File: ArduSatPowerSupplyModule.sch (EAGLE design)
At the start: 167 parts, among them IC1 AVR-MEGA8-MI, IC10 TMP102, IC11 TMP102, IC2 ATMEGA16U2-MU, IC3 LTC3115, IC4 LTC4078, IC5 MAX17043G+U, IC6 MAX4372F, IC7 LTC3536, IC8 MAX4372F, IC9 LTC3536, Q1 RJU003N03 N-MOSFET, Q2 RJU003N03 N-MOSFET, Q3 MOSFET-PCHANNELSMT2, Q4 RJU003N03 N-MOSFET, Q5 RJU003N03 N-MOSFET, Q6 RJU003N03 N-MOSFET, Q7 RJU003N03 N-MOSFET, Q8 RJU003N03 N-MOSFET, Q9 RJU003N03 N-MOSFET, SW1 RESET, SW2 SWITCH-SPDT

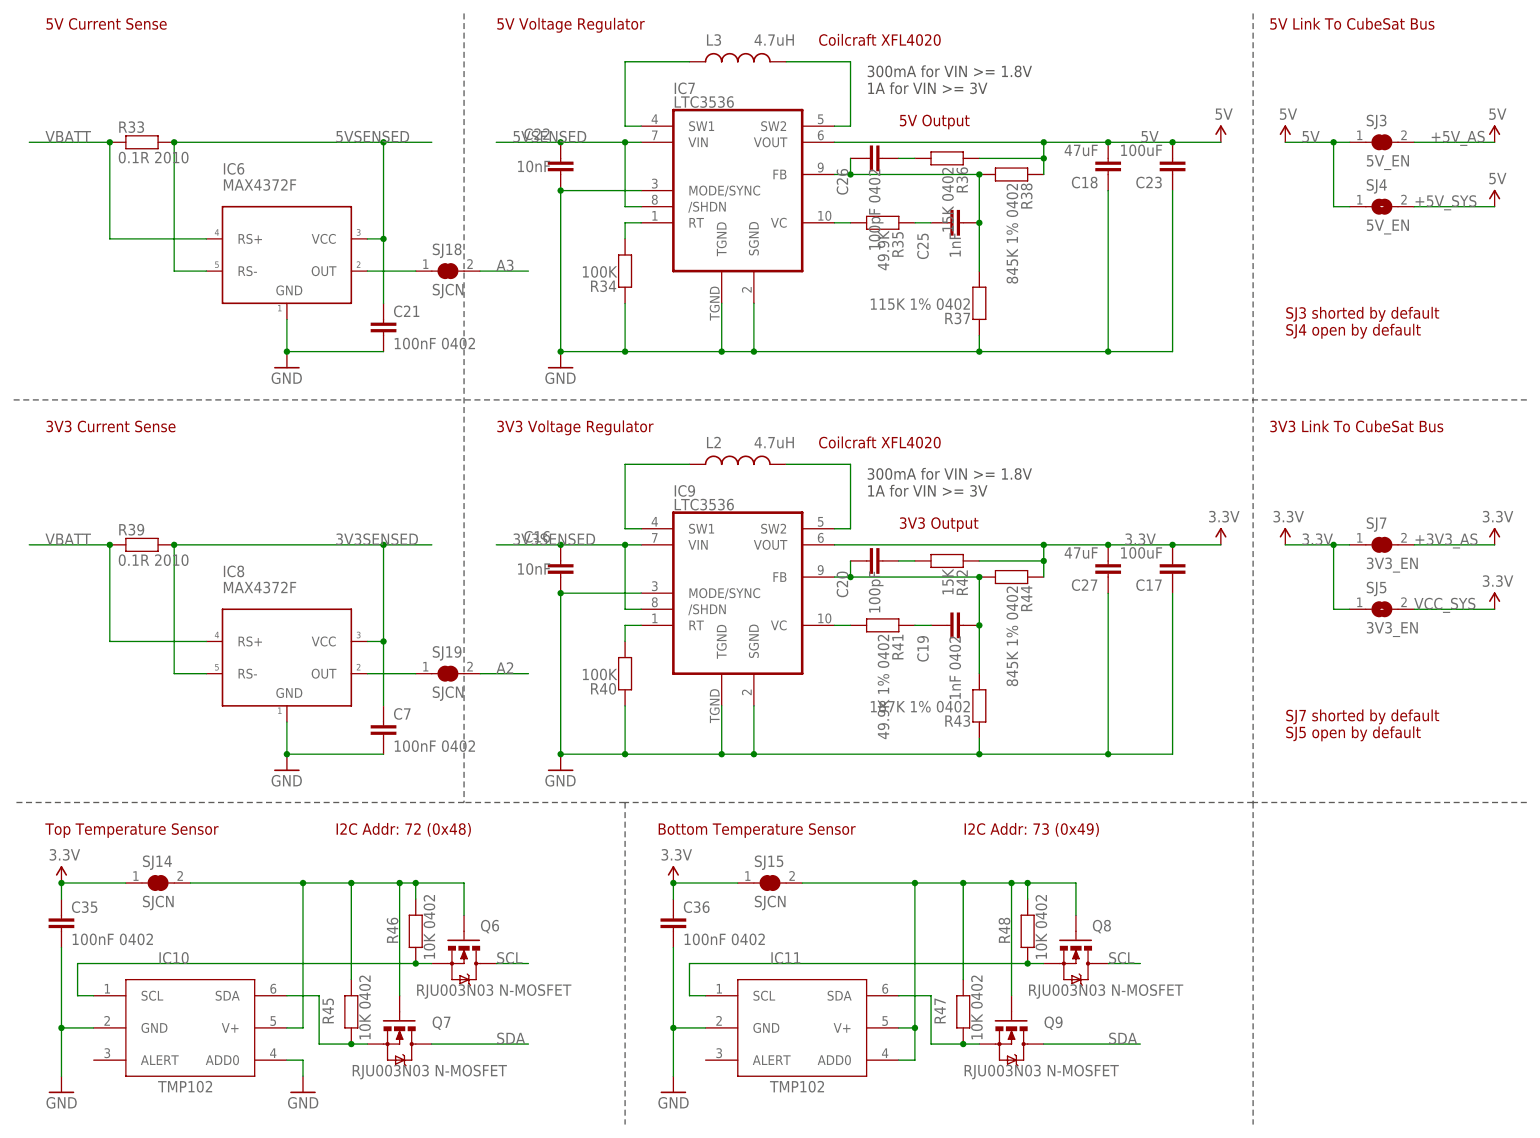
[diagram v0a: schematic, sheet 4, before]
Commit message: Changed max charge rate to 1A; removed solder jumpers for ArduSat power pins
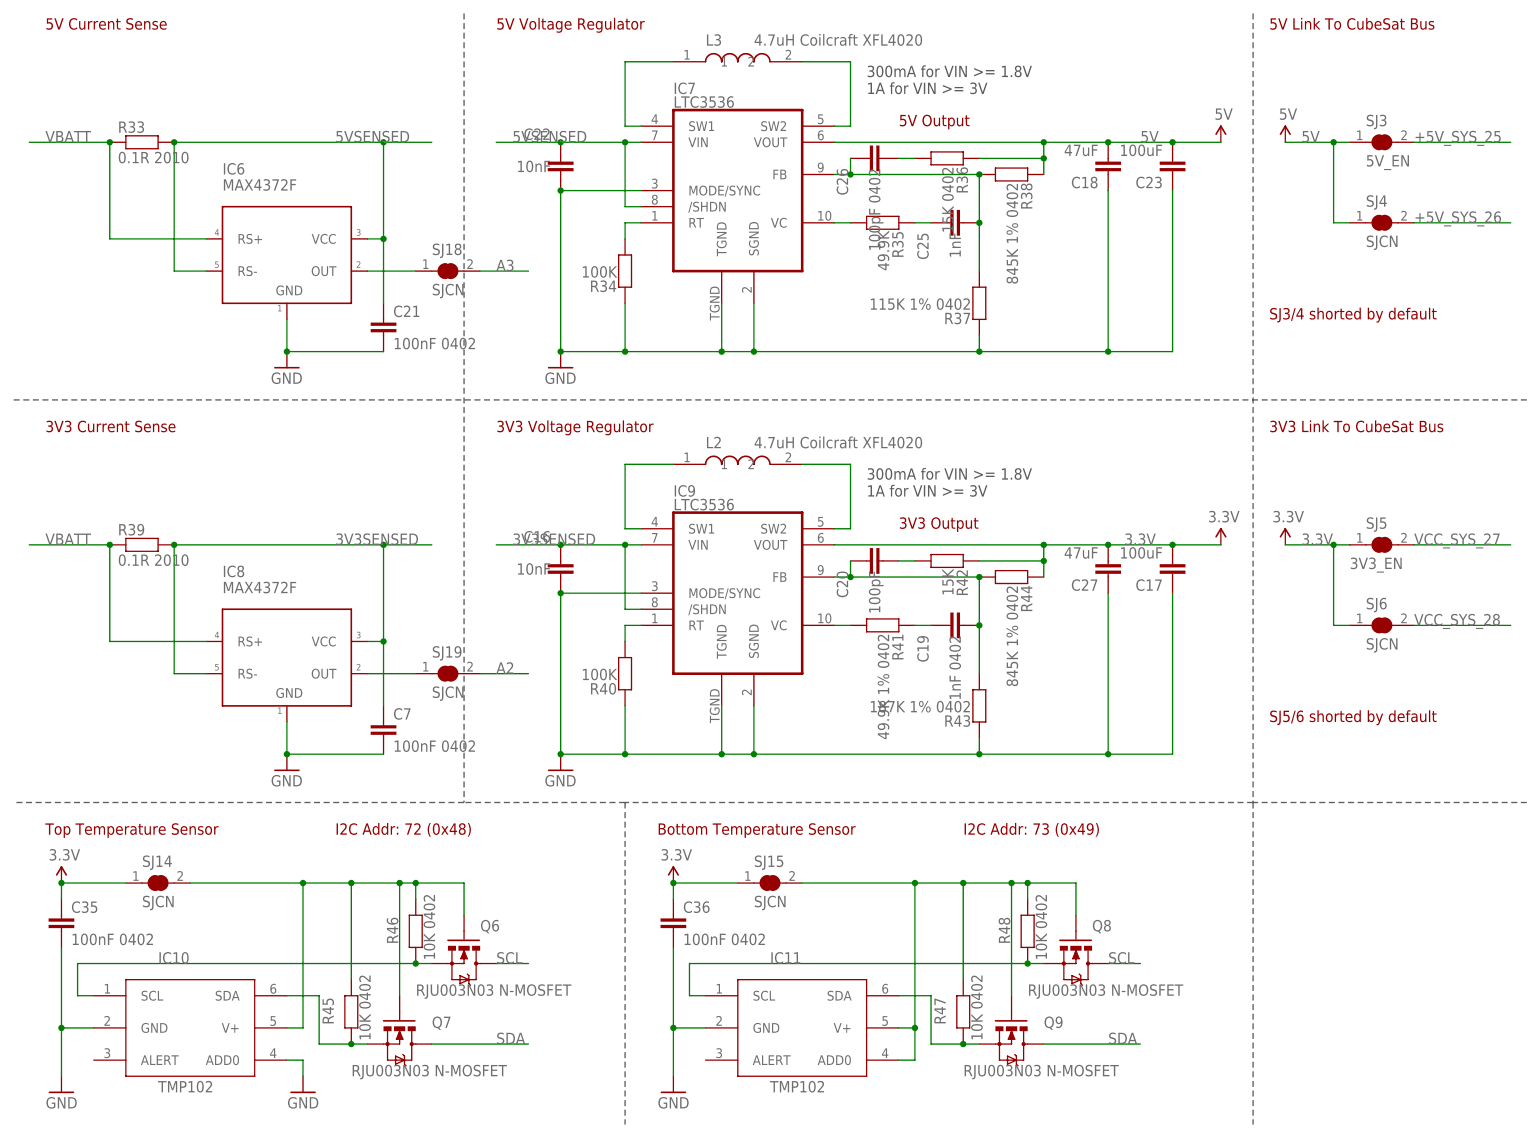
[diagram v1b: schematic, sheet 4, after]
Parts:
- C12, C34: value 1uF 0603 -> 1uF 0402
- IC1: value AVR-MEGA8-MI -> ATmega328P
- L1: device freetronics-jon:INDUCTOR -> freetronics-jon:INDUCTORCDRH
- L2, L3: value 4.7uH -> 4.7uH Coilcraft XFL4020; device freetronics-luke:INDUCTOR -> freetronics-jon:INDUCTOR
- L4: device freetronics-master-v1:INDUCTOR0805-LARGE -> freetronics-master-v1.1:INDUCTOR0805-LARGE
- R21: value 1.05K 1% 0603 -> 1K 1% 0402
- R22: value 1.18K 1% 0603 -> 1K 1% 0402
- R24: value 10K 0603 -> 10K 0402
- SJ4: value 5V_EN -> SJCN; device freetronics-master-v1.1:SJ -> freetronics-jon:SJCN
- SJ5: device freetronics-master-v1.1:SJ -> freetronics-jon:SJCN
- SJ6: value RESET-EN -> SJCN; device freetronics-jon:SJC0402 -> freetronics-jon:SJCN
- SJ7: value 3V3_EN -> RESET-EN; device freetronics-jon:SJCN -> freetronics-jon:SJC0402
- renumbered U$10 to FID1, U$28 to FID2, U$29 to FID3
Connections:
- net D2_SDA renamed D2
- net D3_SCL renamed D3
- removed net +3V3_AS: H1.52, SJ7.2
- removed net +5V_AS: H1.51, SJ3.2
- removed net +5V_SYS: H2.25, H2.26, SJ4.2
- removed net VCC_SYS: H2.27, H2.28, SJ5.2
- new net +5V_SYS_25: H2.25, SJ3.2
- new net +5V_SYS_26: H2.26, SJ4.2
- new net H1_51: H1.51
- new net H1_52: H1.52
- new net VCC_SYS_27: H2.27, SJ5.2
- new net VCC_SYS_28: H2.28, SJ6.2
- net 3.3V: now also SJ6.1; no longer SJ7.1
- net DTR: now also SJ7.1; no longer SJ6.1
- net N$60: now also SJ7.2; no longer SJ6.2
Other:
- note added: "1A max charge"
- note added: "Add I2C isolation onto CubeSat bus Remove I2C isolation from nodes on the board (TMP102, etc)"
- note added: "SJ3/4 shorted by default"
- note added: "SJ5/6 shorted by default"
- note added: "V1.0 (2013-04-29)"
- note removed: "950mA max charge on DCIN 850mA max charge on USBIN"
- note removed: "Coilcraft XFL4020"
- note removed: "SJ3 shorted by default SJ4 open by default"
- note removed: "SJ7 shorted by default SJ5 open by default"
- note removed: "V1.0 (2013-02-24)"

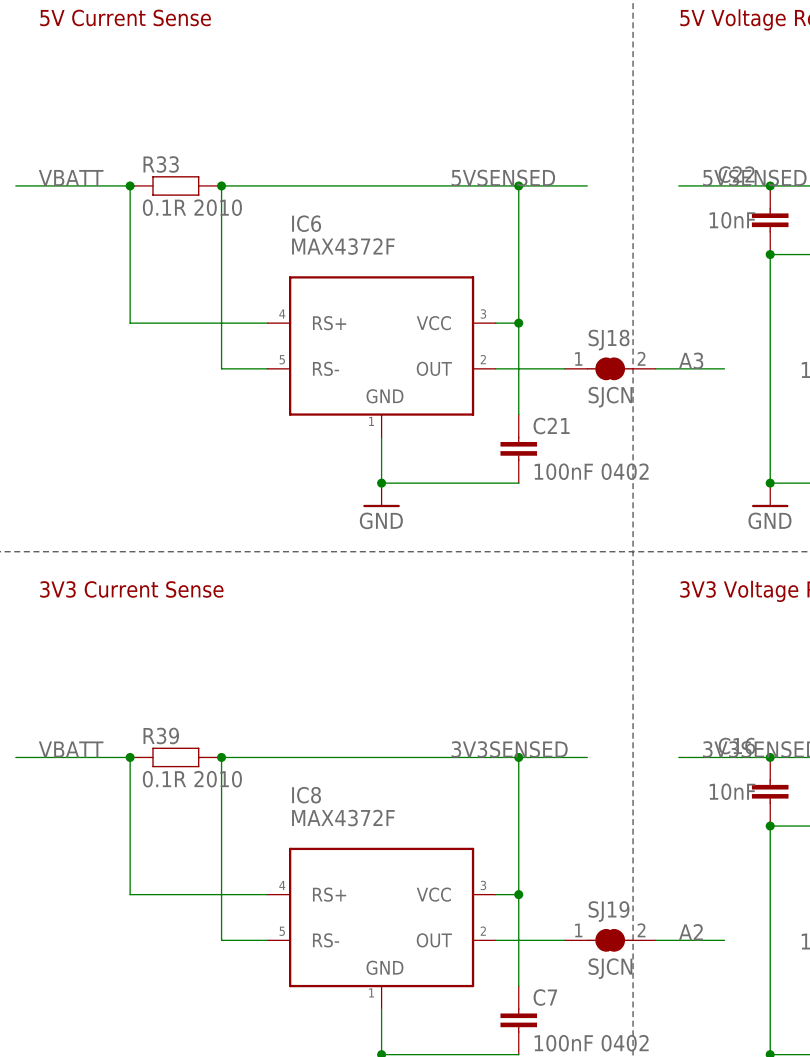
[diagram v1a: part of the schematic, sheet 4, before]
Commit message: Changed current sense chip VCC to 5V
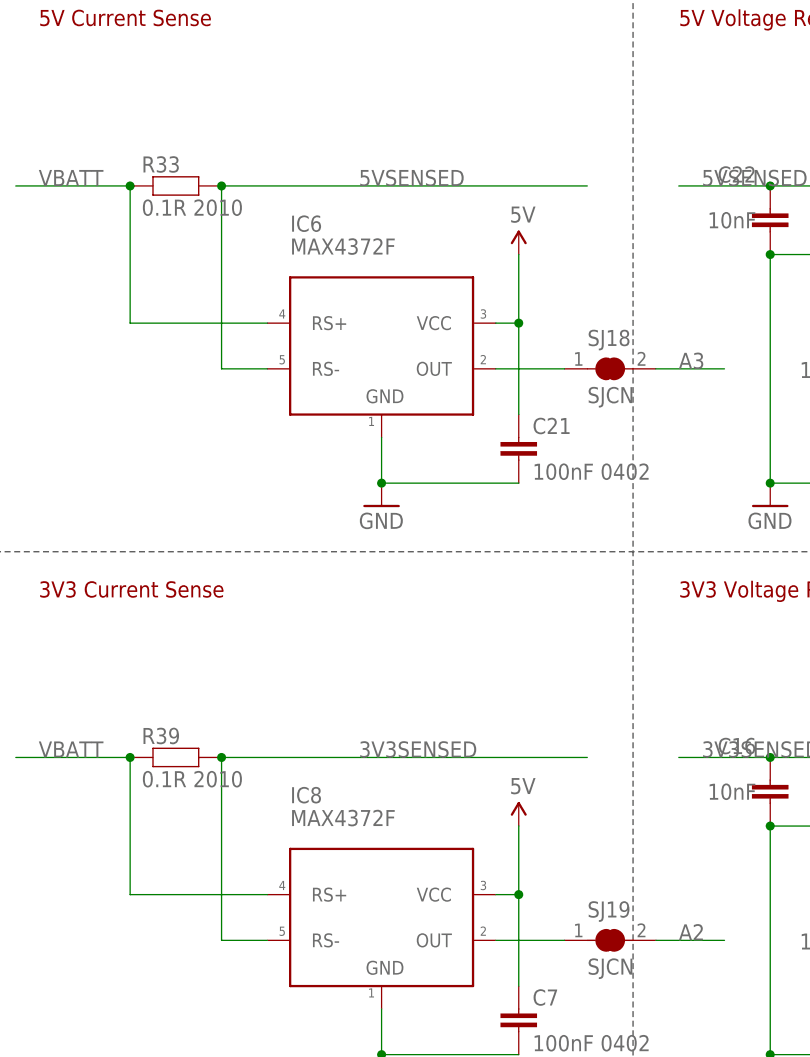
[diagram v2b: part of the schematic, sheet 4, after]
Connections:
- net 3V3SENSED: no longer C7.1, IC8.VCC
- net 5V: now also C21.1, C7.1, IC6.VCC, IC8.VCC
- net 5VSENSED: no longer C21.1, IC6.VCC
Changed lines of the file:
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@@
 <part name="SJ4" library="freetronics-jon" deviceset="SJC" device="N"/>
 <part name="SJ6" library="freetronics-jon" deviceset="SJC" device="N"/>
+<part name="U$3" library="SparkFun" deviceset="5V" device=""/>
+<part name="U$6" library="SparkFun" deviceset="5V" device=""/>
 </parts>
 <sheets>
@@
 <instance part="SJ4" gate="G$1" x="220.98" y="147.32"/>
 <instance part="SJ6" gate="G$1" x="220.98" y="83.82"/>
+<instance part="U$3" gate="G$1" x="63.5" y="152.4"/>
+<instance part="U$6" gate="G$1" x="63.5" y="88.9"/>
 </instances>
 <busses>
@@
 <junction x="187.96" y="160.02"/>
 </segment>
+<segment>
+<pinref part="IC6" gate="G$1" pin="VCC"/>
+<wire x1="60.96" y1="144.78" x2="63.5" y2="144.78" width="0.1524" layer="91"/>
+<pinref part="C21" gate="G$1" pin="1"/>
+<wire x1="63.5" y1="134.62" x2="63.5" y2="144.78" width="0.1524" layer="91"/>
+<pinref part="U$3" gate="G$1" pin="5V"/>
+<wire x1="63.5" y1="152.4" x2="63.5" y2="144.78" width="0.1524" layer="91"/>
+<junction x="63.5" y="144.78"/>
+</segment>
+<segment>
+<pinref part="IC8" gate="G$1" pin="VCC"/>
+<wire x1="60.96" y1="81.28" x2="63.5" y2="81.28" width="0.1524" layer="91"/>
+<pinref part="C7" gate="G$1" pin="1"/>
+<wire x1="63.5" y1="71.12" x2="63.5" y2="81.28" width="0.1524" layer="91"/>
+<pinref part="U$6" gate="G$1" pin="5V"/>
+<wire x1="63.5" y1="88.9" x2="63.5" y2="81.28" width="0.1524" layer="91"/>
+<junction x="63.5" y="81.28"/>
+</segment>
 </net>
 <net name="SDA" class="0">
@@
 <pinref part="R39" gate="G$1" pin="2"/>
 <wire x1="30.48" y1="76.2" x2="30.48" y2="96.52" width="0.1524" layer="91"/>
-<wire x1="30.48" y1="96.52" x2="63.5" y2="96.52" width="0.1524" layer="91"/>
+<wire x1="30.48" y1="96.52" x2="71.12" y2="96.52" width="0.1524" layer="91"/>
 <junction x="30.48" y="96.52"/>
-<pinref part="IC8" gate="G$1" pin="VCC"/>
-<wire x1="60.96" y1="81.28" x2="63.5" y2="81.28" width="0.1524" layer="91"/>
-<pinref part="C7" gate="G$1" pin="1"/>
-<wire x1="63.5" y1="71.12" x2="63.5" y2="81.28" width="0.1524" layer="91"/>
-<wire x1="63.5" y1="81.28" x2="63.5" y2="96.52" width="0.1524" layer="91"/>
-<junction x="63.5" y="81.28"/>
-<wire x1="63.5" y1="96.52" x2="71.12" y2="96.52" width="0.1524" layer="91"/>
-<junction x="63.5" y="96.52"/>
-<label x="55.88" y="96.52" size="1.778" layer="95"/>
+<label x="45.72" y="96.52" size="1.778" layer="95"/>
 </segment>
 <segment>
@@
 <segment>
 <pinref part="R33" gate="G$1" pin="2"/>
-<wire x1="30.48" y1="160.02" x2="63.5" y2="160.02" width="0.1524" layer="91"/>
-<pinref part="C21" gate="G$1" pin="1"/>
-<wire x1="63.5" y1="134.62" x2="63.5" y2="144.78" width="0.1524" layer="91"/>
-<pinref part="IC6" gate="G$1" pin="VCC"/>
-<wire x1="63.5" y1="144.78" x2="63.5" y2="160.02" width="0.1524" layer="91"/>
-<wire x1="60.96" y1="144.78" x2="63.5" y2="144.78" width="0.1524" layer="91"/>
-<junction x="63.5" y="144.78"/>
+<wire x1="30.48" y1="160.02" x2="71.12" y2="160.02" width="0.1524" layer="91"/>
 <pinref part="IC6" gate="G$1" pin="RS-"/>
 <wire x1="35.56" y1="139.7" x2="30.48" y2="139.7" width="0.1524" layer="91"/>
 <wire x1="30.48" y1="139.7" x2="30.48" y2="160.02" width="0.1524" layer="91"/>
 <junction x="30.48" y="160.02"/>
-<wire x1="63.5" y1="160.02" x2="71.12" y2="160.02" width="0.1524" layer="91"/>
-<junction x="63.5" y="160.02"/>
-<label x="55.88" y="160.02" size="1.778" layer="95"/>
+<label x="45.72" y="160.02" size="1.778" layer="95"/>
 </segment>
 </net>

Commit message: Relabelled board from ArduSat to LibreSat
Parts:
- removed Q3: MOSFET-PCHANNELSMT2, freetronics-jon:MOSFET-PCHANNELSMT2
- removed R27: 1K, freetronics-jon:RESISTOR0402
- removed R28: 33K, freetronics-jon:RESISTOR0402
- R11, R25: value 2K2 0402 -> 3K3 0402
- R12, R26: value 1K 0402 -> 1K5 0402
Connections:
- removed net N$4: JP11.2, R27.1
- removed net N$7: Q3.G, R27.2, R28.2
- net A2: no longer SJ19.2
- net A3: no longer SJ18.2
- net A6: now also SJ19.2
- net A7: now also SJ18.2
- net GND: no longer JP10.1
- net N$5: now also JP10.1; no longer Q3.S, R28.1
- net VBATT: now also JP11.2; no longer Q3.D
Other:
- note added: "LibreSat Power Supply Module"
- note added: "SKU: LSPSM"
- note added: "V1.1 (2013-04-29)"
- note added: "www.freetronics.com/lspsm"
- note removed: "ArduSat Power Supply Module"
- note removed: "SKU: ASPSM"
- note removed: "V1.0 (2013-04-29)"
- note removed: "www.freetronics.com/aspsm"
